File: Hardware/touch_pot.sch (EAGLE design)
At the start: 79 parts, among them CON1 SINGLE_PADSMD, CON10 SINGLE_PADSMD, CON11 SINGLE_PADSMD, CON12 SINGLE_PADSMD, CON13 SINGLE_PADSMD, CON14 SINGLE_PADSMD, CON15 SINGLE_PADSMD, CON2 SINGLE_PADSMD, CON3 SINGLE_PADSMD, CON4 SINGLE_PADSMD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

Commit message: Changed all parts to SFE parts with SKUs
Changed all parts to SFE parts with SKUs
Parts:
- removed PB1: (no value), djd_eagle_library:PB_TACT_4SMT
- added S1: SWITCH-MOMENTARY-2SMD, SparkFun-Electromechanical:SWITCH-MOMENTARY-2SMD
- C1, C2, C5, C7: value 10 uF -> 10uF; device SparkFun:CAP_POL1206 -> SparkFun-Capacitors:10UF-16V-10%(TANT)
- C3, C4, C6, C8: value 0.1 uF -> 0.1uF; device djd_eagle_library:C-USSMT0603 -> SparkFun-Capacitors:0.1UF-25V(+80/-20%)(0603)
- D1, D2, D3, D4, D5, D6, D7, D8: value APTR3216SECK -> Green; device djd_eagle_library:LEDREV_32_16 -> SparkFun-LED:LED-GREEN1206-BOTTOM
- R1: value 10 kohm -> 10K; device djd_eagle_library:R-USSMT0603 -> SparkFun-Resistors:10KOHM-1/10W-1%(0603)0603
- R10, R11, R2, R3, R4, R5, R6, R7, R8, R9: value 100 ohm -> 100; device djd_eagle_library:R-USSMT0603 -> SparkFun-Resistors:100OHM-1/10W-1%(0603)
- U3: value 5V_REG_LDOSMD -> 5V; device SparkFun:V_REG_LDOSMD -> SparkFun-PowerIC:V_REG_MIC52055V
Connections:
- net AUX: now also S1.1; no longer PB1.1
- net CPAD1: now also R3.2; no longer R3.1
- net CPAD2: now also R2.2; no longer R2.1
- net GND: now also S1.2; no longer PB1.4
- net N$37: now also R2.1; no longer R2.2
- net N$38: now also R3.1; no longer R3.2
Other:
- moved on the sheet: R2, R3

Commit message: Last push before second round of protos 4 Realz
Lots of QC checklist changes, added parts to SFE library,
isolate, schematic cleanup, added all SFE parts with SKUs.
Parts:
- U1: device djd_eagle_library:PIC16F1829SSOP20 -> SparkFun-DigitalIC:PIC16F1829
- U2: device djd_eagle_library:AD6262TSSOP -> SparkFun-AnalogIC:AD5262

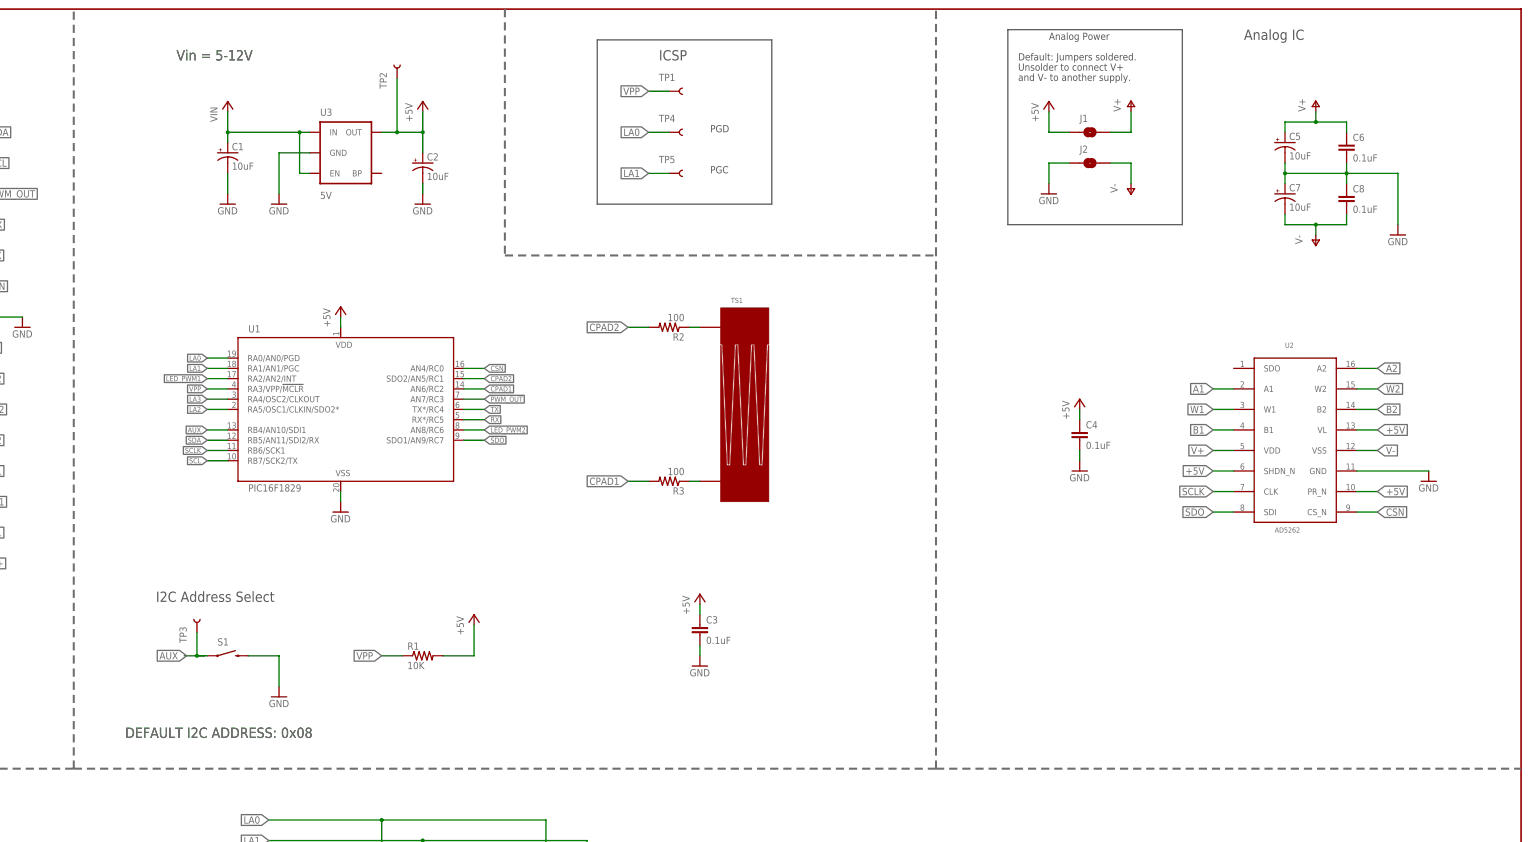
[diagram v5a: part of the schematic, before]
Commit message: Changed pinout to standard I2C pinout
Changed pinout to standard I2C pinout
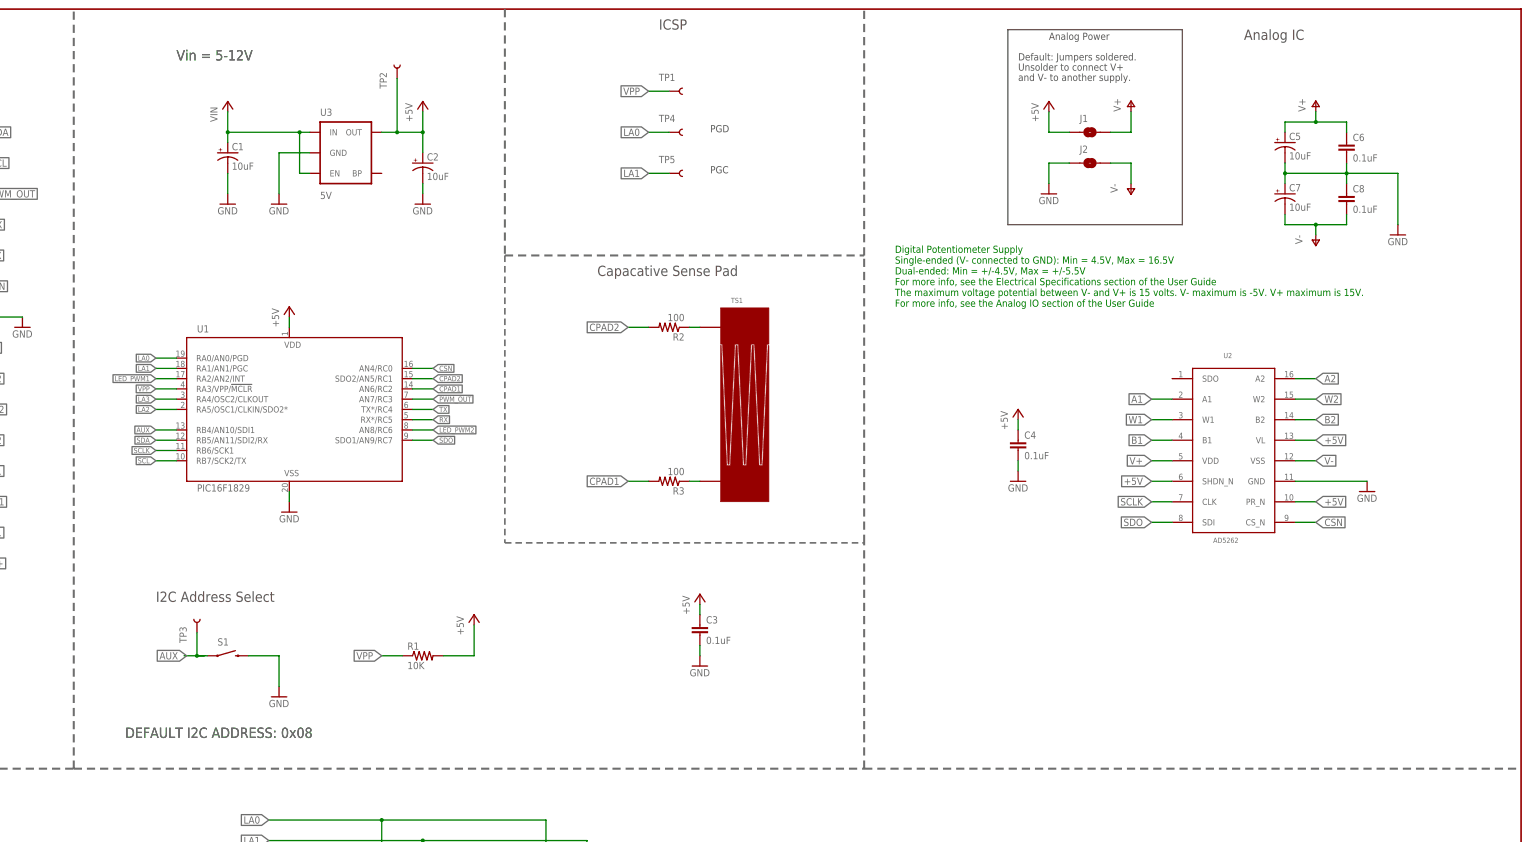
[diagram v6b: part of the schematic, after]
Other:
- note added: "Capacative Sense Pad"
- note added: "Digital Potentiometer Supply Single-ended (V- connected to GND): Min = 4.5V, Max = 16.5V Dual-ended: Min = +/-4.5V, Max = +/-5.5V For more info, see the Electrical Specifications section of the User Guide The maximum voltage potential between V- and V+ is 15 volts. V- maximum is -5V. V+ maximum is 15V. For more info, see the Analog IO section of the User Guide"
- moved on the sheet: C4, U1, U2

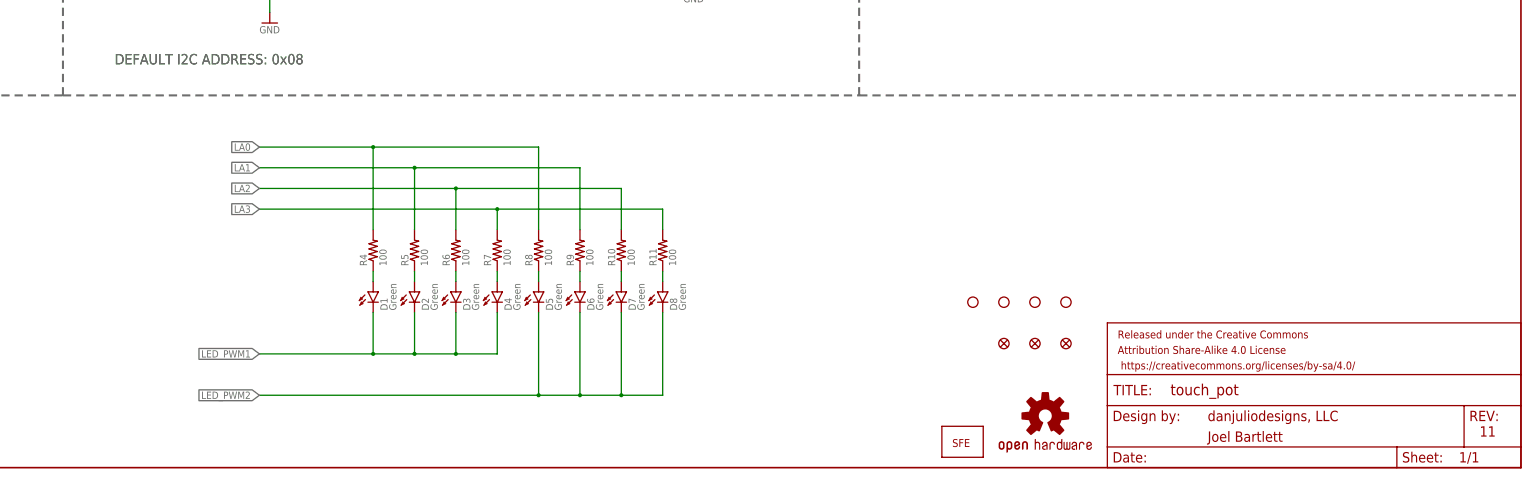
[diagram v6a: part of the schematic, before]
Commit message: Ready for Reds
Added note about Non-plated Thru Holes on the bottom-mounted LEDs,
added note about I2C addressing, added note about maximum and min.
voltages on V+ and V-, moved  VPP test point ever so slightly, added
polarity silk to bottom-mounted LEDs, added note in Sparkle about BLACK
SOLDERMASK.
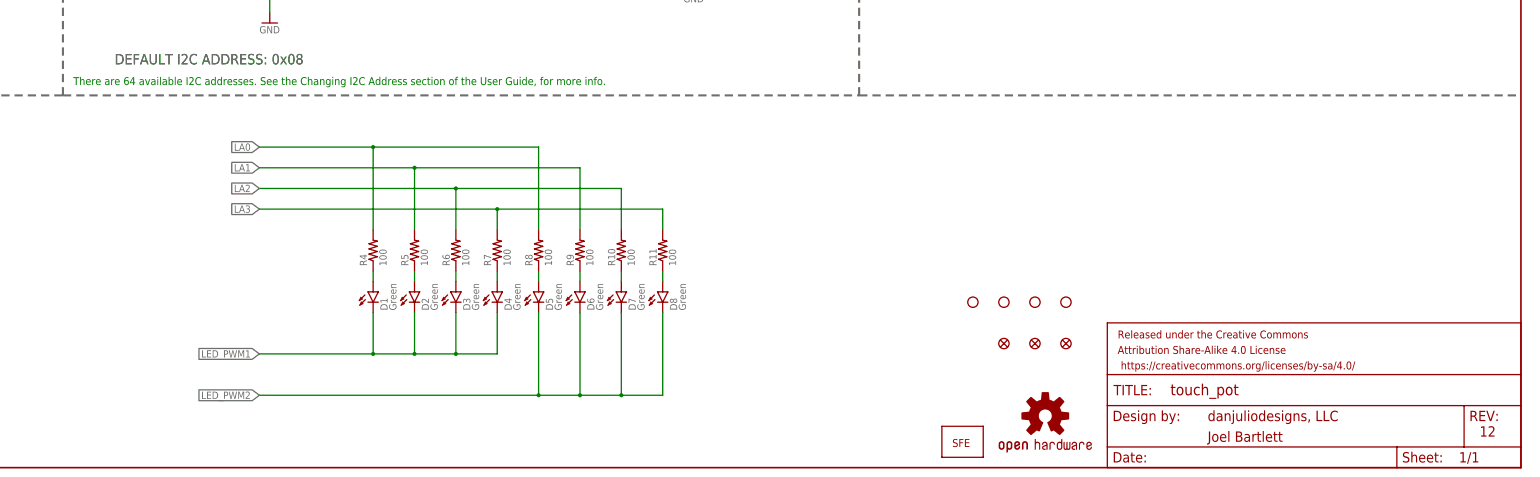
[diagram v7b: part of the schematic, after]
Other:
- note added: "12"
- note added: "There are 64 available I2C addresses. See the Changing I2C Address section of the User Guide, for more info."
- note removed: "11"
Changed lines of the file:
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@@
 <?xml version="1.0" encoding="utf-8"?>
 <!DOCTYPE eagle SYSTEM "eagle.dtd">
-<eagle version="7.1.0">
+<eagle version="7.2.0">
 <drawing>
 <settings>
@@
 <wire x1="347.98" y1="226.06" x2="347.98" y2="274.32" width="0.1524" layer="97"/>
 <text x="354.838" y="11.43" size="2.54" layer="94">danjuliodesigns, LLC</text>
-<text x="421.64" y="7.62" size="2.54" layer="94">11</text>
+<text x="421.64" y="7.62" size="2.54" layer="94">12</text>
 <text x="93.98" y="132.715" size="2.54" layer="97">I2C Address Select</text>
 <text x="22.86" y="264.16" size="2.54" layer="97">IO Connections</text>
@@
 <wire x1="180.34" y1="147.32" x2="269.24" y2="147.32" width="0.4064" layer="95" style="longdash"/>
 <text x="203.2" y="213.36" size="2.54" layer="97">Capacative Sense Pad</text>
+<text x="76.2" y="93.98" size="1.9304" layer="91">There are 64 available I2C addresses. See the Changing I2C Address section of the User Guide, for more info.  </text>
 </plain>
 <instances>

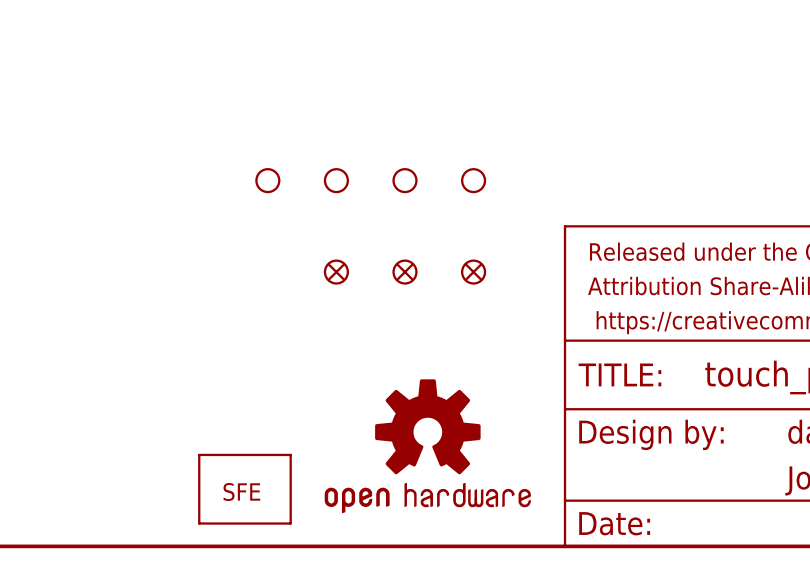
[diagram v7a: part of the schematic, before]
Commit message: replaced fids with SFE fids
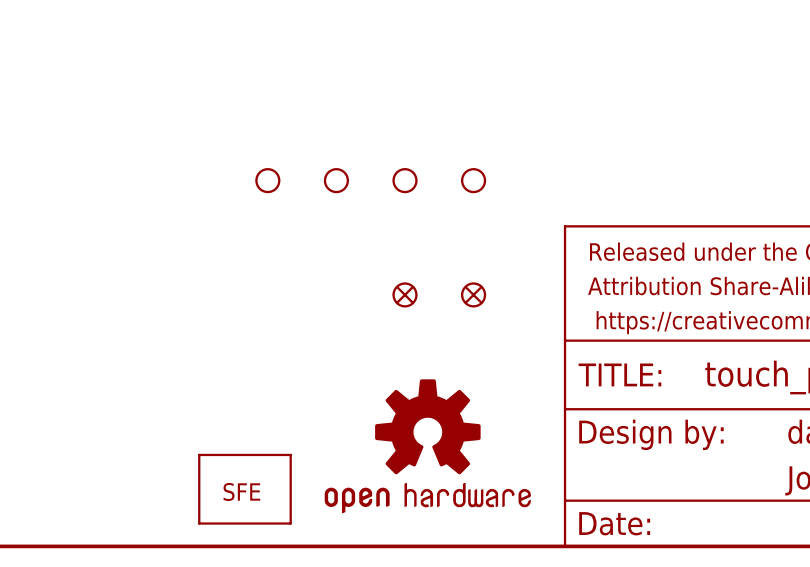
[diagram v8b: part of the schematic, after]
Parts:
- removed U$1, U$2, U$3: FIDUCIAL, djd_eagle_library:FIDUCIAL
- added FID1, FID2: FIDUCIAL1X2, SparkFun-Aesthetics:FIDUCIAL1X2
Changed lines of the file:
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@@
 <?xml version="1.0" encoding="utf-8"?>
 <!DOCTYPE eagle SYSTEM "eagle.dtd">
-<eagle version="7.2.0">
+<eagle version="6.6.0">
 <drawing>
 <settings>
@@
 <part name="P+2" library="supply1" deviceset="V+" device=""/>
 <part name="P-1" library="supply1" deviceset="V-" device=""/>
-<part name="U$1" library="djd_eagle_library" deviceset="FIDUCIAL" device=""/>
 <part name="TS1" library="djd_eagle_library" deviceset="2CH_LINEAR_TOUCH" device=""/>
 <part name="CON1" library="djd_eagle_library" deviceset="SINGLE_PAD" device="SMD" value=""/>
@@
 <part name="P+5" library="supply1" deviceset="+5V" device=""/>
 <part name="GND5" library="supply1" deviceset="GND" device=""/>
-<part name="U$2" library="djd_eagle_library" deviceset="FIDUCIAL" device=""/>
-<part name="U$3" library="djd_eagle_library" deviceset="FIDUCIAL" device=""/>
 <part name="P+6" library="supply1" deviceset="+5V" device=""/>
 <part name="GND6" library="supply1" deviceset="GND" device=""/>
@@
 <part name="U1" library="SparkFun-DigitalIC" deviceset="PIC16F1829" device=""/>
 <part name="U2" library="SparkFun-AnalogIC" deviceset="AD5262" device=""/>
+<part name="FID1" library="SparkFun-Aesthetics" deviceset="FIDUCIAL" device="1X2"/>
+<part name="FID2" library="SparkFun-Aesthetics" deviceset="FIDUCIAL" device="1X2"/>
 </parts>
 <sheets>
@@
 <instance part="P+2" gate="1" x="381" y="256.54"/>
 <instance part="P-1" gate="1" x="381" y="220.98"/>
-<instance part="U$1" gate="G$1" x="304.8" y="30.48"/>
 <instance part="TS1" gate="G$1" x="233.68" y="157.48"/>
 <instance part="CON1" gate="G$1" x="43.18" y="251.46" rot="R90"/>
@@
 <instance part="P+5" gate="1" x="228.6" y="134.62"/>
 <instance part="GND5" gate="1" x="401.32" y="223.52"/>
-<instance part="U$2" gate="G$1" x="312.42" y="30.48"/>
-<instance part="U$3" gate="G$1" x="320.04" y="30.48"/>
 <instance part="P+6" gate="1" x="172.72" y="129.54"/>
 <instance part="GND6" gate="1" x="124.46" y="109.22"/>
@@
 <instance part="U1" gate="1" x="127" y="177.8"/>
 <instance part="U2" gate="1" x="360.68" y="170.18"/>
+<instance part="FID1" gate="G$1" x="320.04" y="27.94"/>
+<instance part="FID2" gate="G$1" x="312.42" y="27.94"/>
 </instances>
 <busses>
